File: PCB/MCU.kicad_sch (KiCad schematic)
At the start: 15 parts, among them J200 2171790001, J201 2086-1104, U200 ESP32-S3-WROOM-1, U201 USBLC6-2SC6

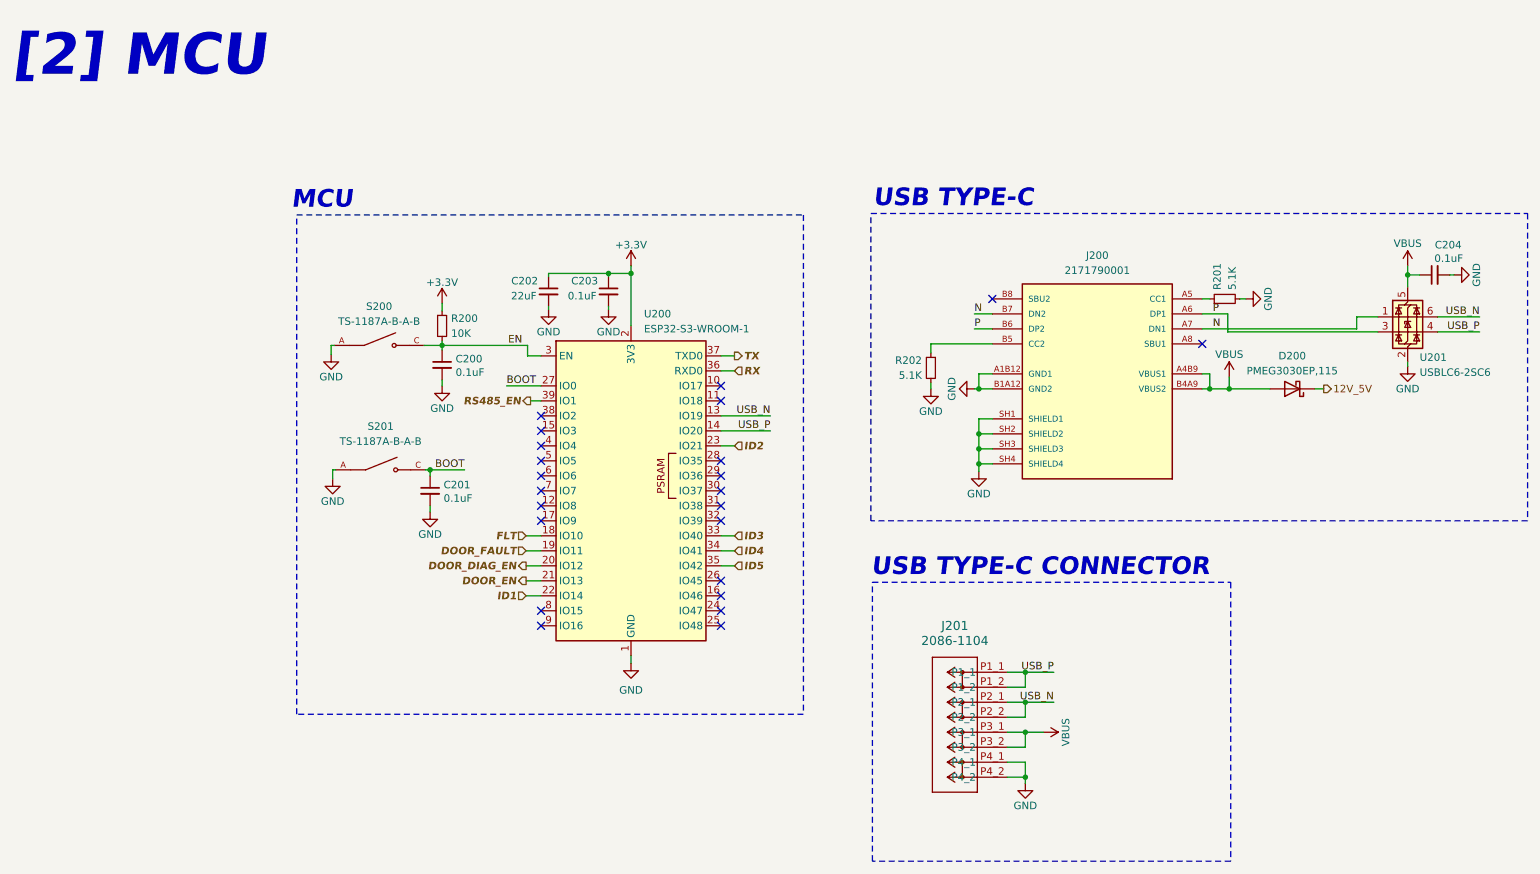
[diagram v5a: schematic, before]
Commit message: Change Placement
Se ha cambiado el placement total para obtener una mejor posicion de conexion de los perifericos
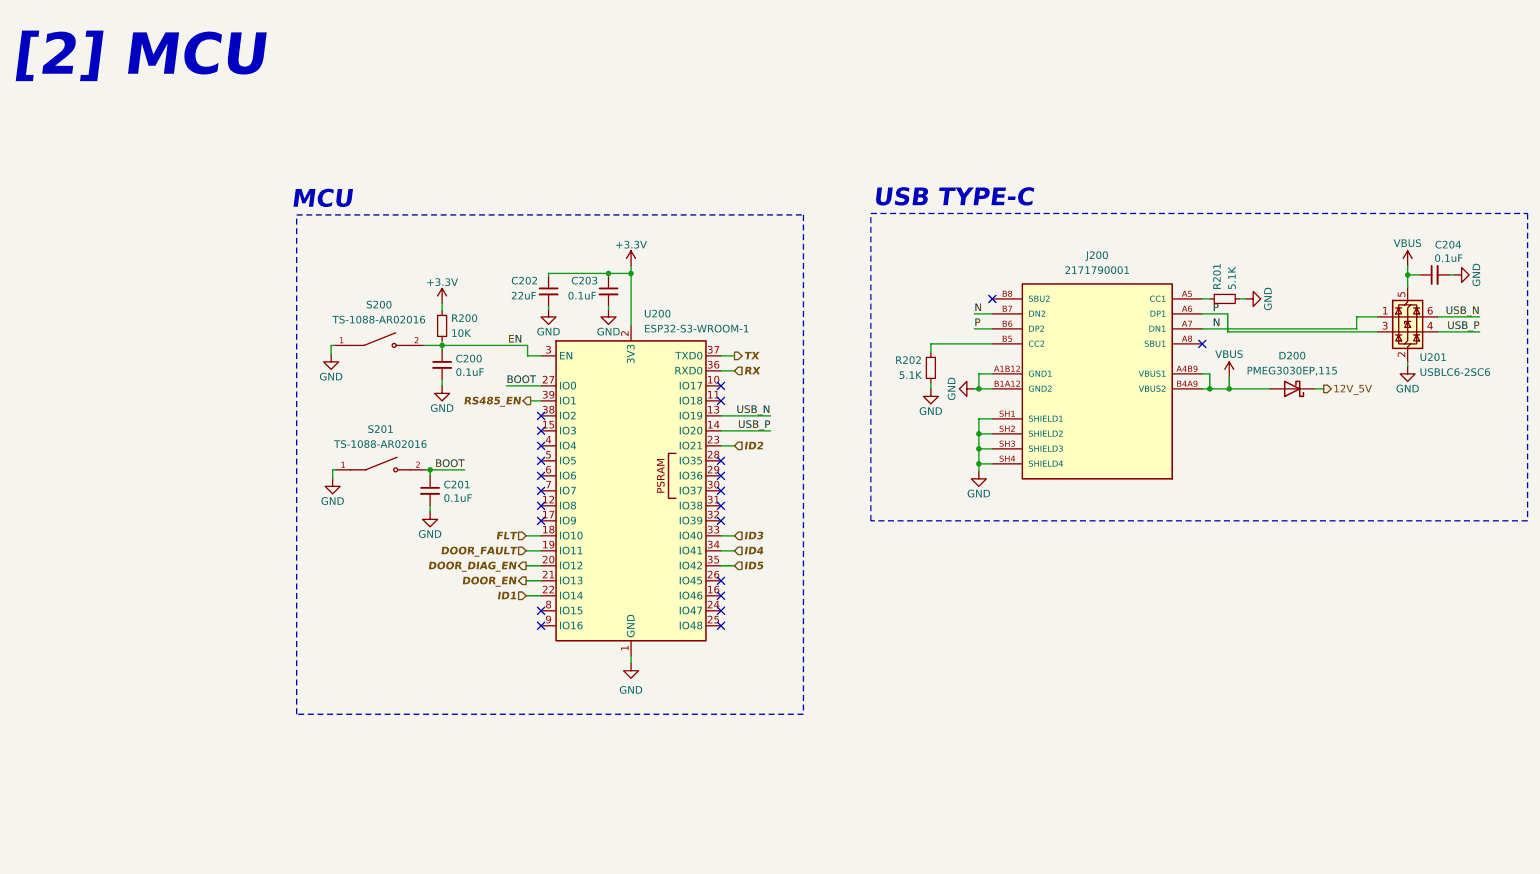
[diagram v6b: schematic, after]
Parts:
- removed J201: 2086-1104, 2086-1104-THT:2086-1104-THT, symbol 2086-1104-THT:2086-1104
- removed S200, S201: TS-1187A-B-A-B, TS-1187A-B-A-B:TS-1187A-B-A-B, symbol TS-1187A-B-A-B:TS-1187A-B-A-B
- added S200, S201: TS-1088-AR02016, TS-1088-AR02016:TS-1088-AR02016, symbol TS-1088-AR02016:TS-1088-AR02016
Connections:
- net BOOT: now also S201.2
- net EN: now also S200.2
- net GND: now also S200.1, S201.1
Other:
- note removed: "USB TYPE-C CONNECTOR"
